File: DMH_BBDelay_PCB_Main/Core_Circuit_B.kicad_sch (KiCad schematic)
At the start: 76 parts, among them J30 Conn_01x08, J31 Conn_01x08, J32 Conn_01x08, J33 Conn_01x08, Q8 J113, SW1 SW_DPDT_3way_x2, SW2 SW_DPDT_x2, SW4 SW_SPDT, U18 CD4053B, U5 TL074, U6 TL074, U7 V3205, U8 CD4046, U9 40106

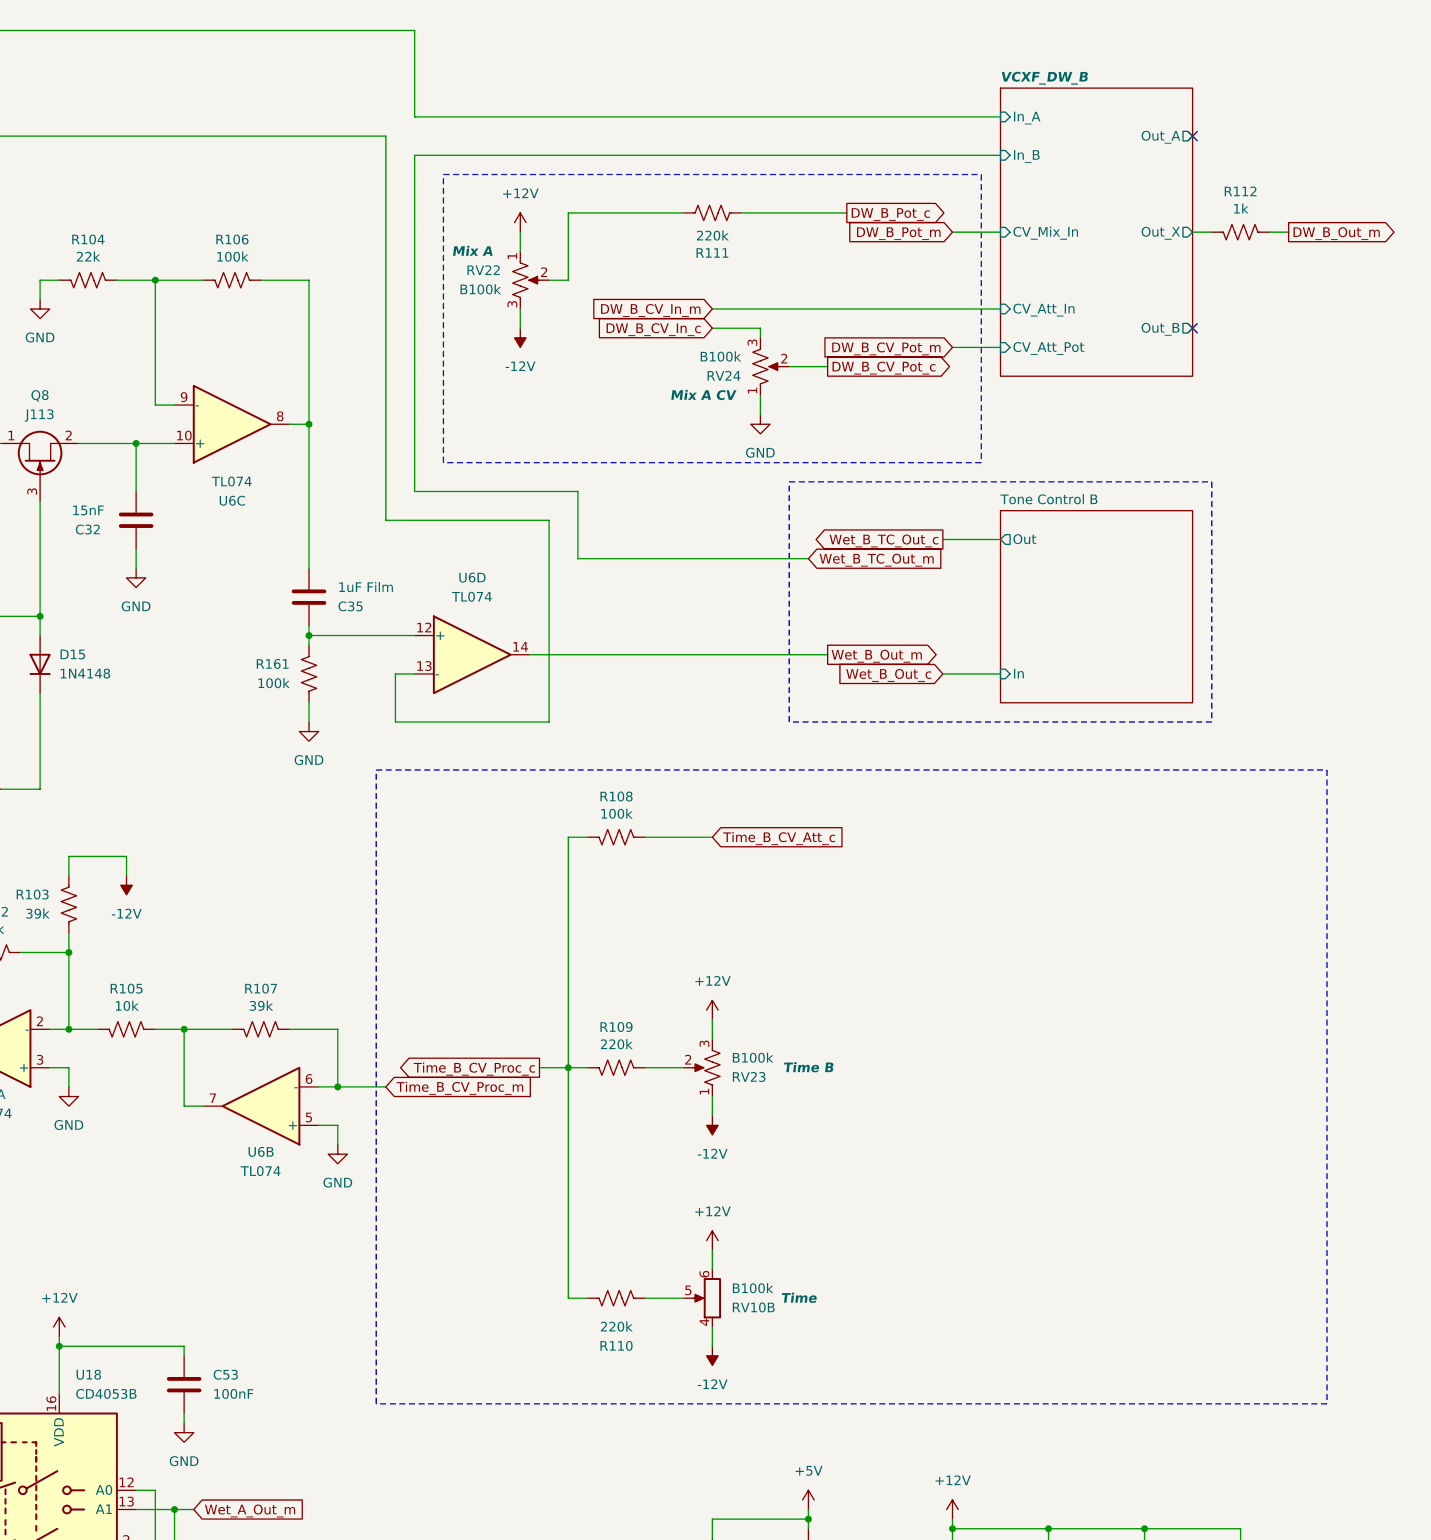
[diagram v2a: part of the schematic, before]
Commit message: Added output filter to channel B
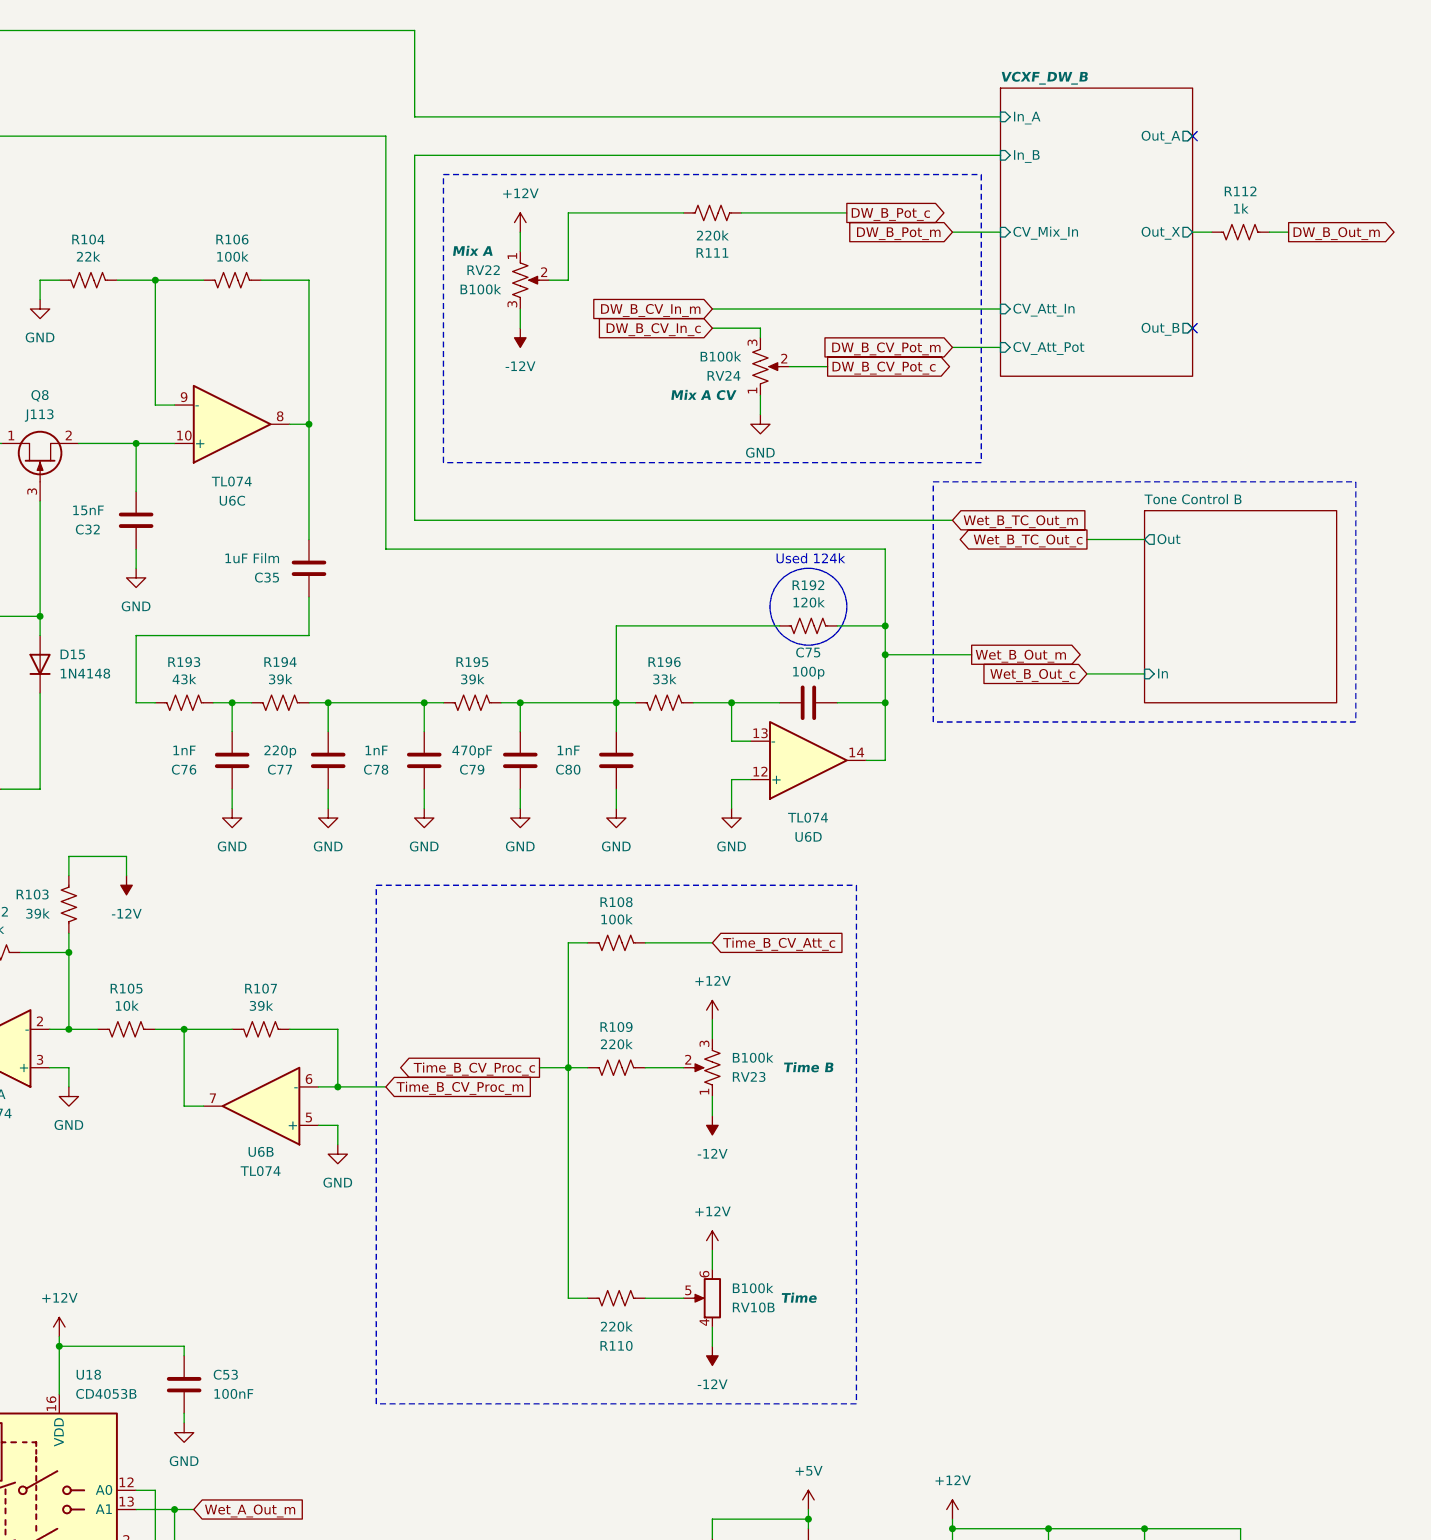
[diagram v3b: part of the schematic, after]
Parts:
- removed R161: 100k, Resistor_THT:R_Axial_DIN0207_L6.3mm_D2.5mm_P7.62mm_Horizontal, symbol Device:R_US
- added C75: 100p, Capacitor_THT:C_Disc_D3.0mm_W2.0mm_P2.50mm, symbol Device:C
- added C76, C78, C80: 1nF, Capacitor_THT:C_Disc_D4.3mm_W1.9mm_P5.00mm, symbol Device:C
- added C77: 220p, Capacitor_THT:C_Disc_D4.3mm_W1.9mm_P5.00mm, symbol Device:C
- added C79: 470pF, Capacitor_THT:C_Disc_D4.3mm_W1.9mm_P5.00mm, symbol Device:C
- added R192: 120k, Resistor_THT:R_Axial_DIN0207_L6.3mm_D2.5mm_P7.62mm_Horizontal, symbol Device:R_US
- added R193: 43k, Resistor_THT:R_Axial_DIN0207_L6.3mm_D2.5mm_P7.62mm_Horizontal, symbol Device:R_US
- added R194, R195: 39k, Resistor_THT:R_Axial_DIN0207_L6.3mm_D2.5mm_P7.62mm_Horizontal, symbol Device:R_US
- added R196: 33k, Resistor_THT:R_Axial_DIN0207_L6.3mm_D2.5mm_P7.62mm_Horizontal, symbol Device:R_US
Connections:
- net GND: now also U6.12 (+), C76.1, C77.1, C78.1, C79.1, C80.1
- net Wet_B_Out_m: now also C75.2, R192.2; no longer U6.13 (-)
- net at C35.1: now also R193.1; no longer U6.12 (+)
- new net: C79.2, C80.2, R192.1, R195.2, R196.1
- new net: C75.1, R196.2, U6.13 (-)
- new net: C77.2, C78.2, R194.2, R195.1
- new net: C76.2, R193.2, R194.1
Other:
- note added: "Used 124k"
- moved on the sheet: C35, R108, U6D

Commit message: Updated internal gains
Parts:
- R104: value 22k -> 18k
- R106: value 100k -> 120k
- R26: value 82k -> 100k
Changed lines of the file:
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@@
 		)
 	)
+	(circle
+		(center 253.746 49.276)
+		(radius 5.08)
+		(stroke
+			(width 0)
+			(type default)
+		)
+		(fill
+			(type none)
+		)
+	)
 	(rectangle
 		(start 45.72 106.68)
@@
 	(text "Used 124k"
 		(exclude_from_sim no)
+		(at 254 43.18 0)
+		(effects
+			(font
+				(size 1.27 1.27)
+			)
+		)
+	)
+	(text "Used 124k"
+		(exclude_from_sim no)
 		(at 330.454 87.884 0)
 		(effects
@@
 			)
 		)
-		(property "Value" "82k"
+		(property "Value" "100k"
 			(at 73.66 77.4699 0)
 			(show_name no)
@@
 			)
 		)
-		(property "Value" "22k"
+		(property "Value" "18k"
 			(at 234.95 47.752 90)
 			(show_name no)
@@
 			)
 		)
-		(property "Value" "100k"
+		(property "Value" "120k"
 			(at 254 47.752 90)
 			(show_name no)

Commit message: Inverted time and tone control pots
... and added AC coupling to the outputs
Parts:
- added C82: 1uF Film, Capacitor_THT:C_Disc_D7.5mm_W5.0mm_P5.00mm, symbol Device:C
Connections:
- net +12V: now also RV10.4, RV23.1; no longer RV10.6, RV23.3
- net -12V: now also RV10.6, RV23.3; no longer RV10.4, RV23.1
- net VCXF_DW_B/Out_X: now also C82.1; no longer R112.1
- new net: C82.2, R112.1
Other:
- moved on the sheet: R112, RV10B, RV23
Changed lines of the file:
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@@
 	(wire
 		(pts
+			(xy 391.16 44.45) (xy 396.24 44.45)
+		)
+		(stroke
+			(width 0)
+			(type default)
+		)
+	)
+	(wire
+		(pts
 			(xy 184.15 162.56) (xy 184.15 165.1)
 		)
@@
 	(wire
 		(pts
-			(xy 381 44.45) (xy 383.54 44.45)
-		)
-		(stroke
-			(width 0)
-			(type default)
-		)
-	)
-	(wire
-		(pts
 			(xy 165.1 31.75) (xy 171.45 31.75)
 		)
@@
 	(wire
 		(pts
-			(xy 391.16 44.45) (xy 393.7 44.45)
-		)
-		(stroke
-			(width 0)
-			(type default)
-		)
-	)
-	(wire
-		(pts
 			(xy 198.12 198.12) (xy 198.12 203.2)
 		)
@@
 	(wire
 		(pts
+			(xy 406.4 50.8) (xy 406.4 44.45)
+		)
+		(stroke
+			(width 0)
+			(type default)
+		)
+	)
+	(wire
+		(pts
 			(xy 177.8 80.01) (xy 177.8 82.55)
 		)
@@
 	(wire
 		(pts
+			(xy 393.7 57.15) (xy 391.16 57.15)
+		)
+		(stroke
+			(width 0)
+			(type default)
+		)
+	)
+	(wire
+		(pts
 			(xy 110.49 111.76) (xy 113.03 111.76)
 		)
@@
 	(wire
 		(pts
+			(xy 381 44.45) (xy 383.54 44.45)
+		)
+		(stroke
+			(width 0)
+			(type default)
+		)
+	)
+	(wire
+		(pts
 			(xy 139.7 31.75) (xy 76.2 31.75)
 		)
@@
 	(wire
 		(pts
+			(xy 391.16 50.8) (xy 406.4 50.8)
+		)
+		(stroke
+			(width 0)
+			(type default)
+		)
+	)
+	(wire
+		(pts
 			(xy 184.15 102.87) (xy 186.69 102.87)
 		)
@@
 	(wire
 		(pts
+			(xy 391.16 57.15) (xy 391.16 50.8)
+		)
+		(stroke
+			(width 0)
+			(type default)
+		)
+	)
+	(wire
+		(pts
 			(xy 304.8 118.11) (xy 304.8 120.65)
 		)
@@
 	(wire
 		(pts
+			(xy 403.86 44.45) (xy 406.4 44.45)
+		)
+		(stroke
+			(width 0)
+			(type default)
+		)
+	)
+	(wire
+		(pts
 			(xy 107.95 71.12) (xy 107.95 67.31)
 		)
@@
 	(global_label "DW_B_Out_m"
 		(shape output)
-		(at 393.7 44.45 0)
+		(at 393.7 57.15 0)
 		(fields_autoplaced yes)
 		(effects
@@
 		)
 		(property "Intersheetrefs" "${INTERSHEET_REFS}"
-			(at 408.2965 44.45 0)
+			(at 408.2965 57.15 0)
 			(hide yes)
 			(show_name no)
@@
 	(symbol
 		(lib_id "Device:R_Potentiometer_US")
-		(at 317.5 154.94 180)
+		(at 317.5 154.94 0)
+		(mirror y)
 		(unit 1)
 		(body_style 1)
@@
 		(dnp no)
 		(property "Reference" "RV23"
-			(at 320.04 156.2101 0)
+			(at 320.04 153.6699 0)
 			(show_name no)
 			(do_not_autoplace no)
@@
 		)
 		(property "Value" "B100k"
-			(at 320.04 153.6701 0)
+			(at 320.04 156.2099 0)
 			(show_name no)
 			(do_not_autoplace no)
@@
 	)
 	(symbol
+		(lib_id "Device:C")
+		(at 387.35 44.45 90)
+		(unit 1)
+		(body_style 1)
+		(exclude_from_sim no)
+		(in_bom yes)
+		(on_board yes)
+		(in_pos_files yes)
+		(dnp no)
+		(property "Reference" "C82"
+			(at 387.35 37.846 90)
+			(show_name no)
+			(do_not_autoplace no)
+			(effects
+				(font
+					(size 1.27 1.27)
+				)
+			)
+		)
+		(property "Value" "1uF Film"
+			(at 387.35 40.386 90)
+			(show_name no)
+			(do_not_autoplace no)
+			(effects
+				(font
+					(size 1.27 1.27)
+				)
+			)
+		)
+		(property "Footprint" "Capacitor_THT:C_Disc_D7.5mm_W5.0mm_P5.00mm"
+			(at 391.16 43.4848 0)
+			(hide yes)
+			(show_name no)
+			(do_not_autoplace no)
+			(effects
+				(font
+					(size 1.27 1.27)
+				)
+			)
+		)
+		(property "Datasheet" ""
+			(at 387.35 44.45 0)
+			(hide yes)
+			(show_name no)
+			(do_not_autoplace no)
+			(effects
+				(font
+					(size 1.27 1.27)
+				)
+			)
+		)
+		(property "Description" "Unpolarized capacitor"
+			(at 387.35 44.45 0)
+			(hide yes)
+			(show_name no)
+			(do_not_autoplace no)
+			(effects
+				(font
+					(size 1.27 1.27)
+				)
+			)
+		)
+		(property "Function" ""
+			(at 387.35 44.45 0)
+			(show_name no)
+			(do_not_autoplace no)
+			(effects
+				(font
+					(size 1.27 1.27)
+				)
+			)
+		)
+		(pin "1"
+		)
+		(pin "2"
+		)
+		(instances
+			(project "DMH_BBDelay_PCB_Main"
+				(path "/58f4306d-5387-4983-bb08-41a2313fd315/53120047-129a-4e0f-876f-6cafa2f18733"
+					(reference "C82")
+					(unit 1)
+				)
+			)
+		)
+	)
+	(symbol
 		(lib_id "Switch:SW_SPDT")
 		(at 96.52 144.78 180)
@@
 	(symbol
 		(lib_id "Device:R_US")
-		(at 387.35 44.45 90)
+		(at 400.05 44.45 90)
 		(mirror x)
 		(unit 1)
@@
 		(dnp no)
 		(property "Reference" "R112"
-			(at 387.35 39.116 90)
+			(at 400.05 39.116 90)
 			(show_name no)
 			(do_not_autoplace no)
@@
 		)
 		(property "Value" "1k"
-			(at 387.35 41.402 90)
+			(at 400.05 41.402 90)
 			(show_name no)
 			(do_not_autoplace no)
@@
 		)
 		(property "Footprint" "Resistor_THT:R_Axial_DIN0207_L6.3mm_D2.5mm_P7.62mm_Horizontal"
-			(at 387.604 45.466 90)
+			(at 400.304 45.466 90)
 			(hide yes)
 			(show_name no)
@@
 		)
 		(property "Datasheet" ""
-			(at 387.35 44.45 0)
+			(at 400.05 44.45 0)
 			(hide yes)
 			(show_name no)
@@
 		)
 		(property "Description" "Resistor, US symbol"
-			(at 387.35 44.45 0)
+			(at 400.05 44.45 0)
 			(hide yes)
 			(show_name no)
@@
 	(symbol
 		(lib_id "Device:R_Potentiometer_Dual_Separate")
-		(at 317.5 185.42 180)
+		(at 317.5 185.42 0)
+		(mirror y)
 		(unit 2)
 		(body_style 1)
@@
 		(dnp no)
 		(property "Reference" "RV10"
-			(at 320.04 186.6901 0)
+			(at 320.04 184.1499 0)
 			(show_name no)
 			(do_not_autoplace no)
@@
 		)
 		(property "Value" "B100k"
-			(at 320.04 184.1501 0)
+			(at 320.04 186.6899 0)
 			(show_name no)
 			(do_not_autoplace no)

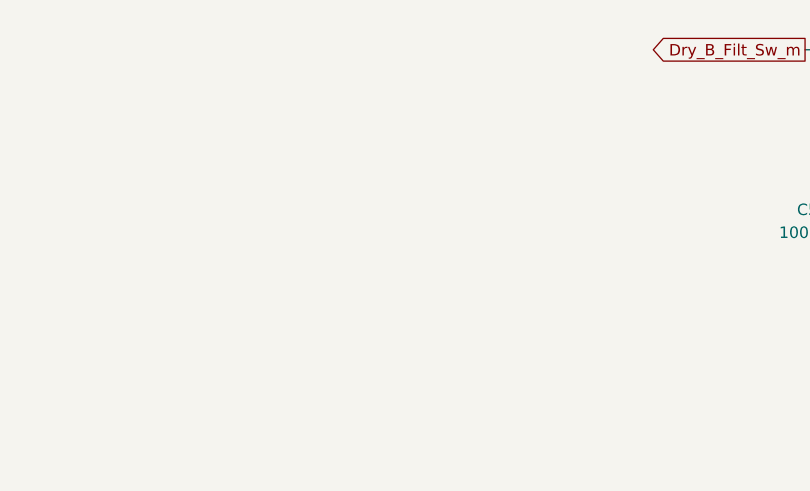
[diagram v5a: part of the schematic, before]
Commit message: Designed input compressor circuits
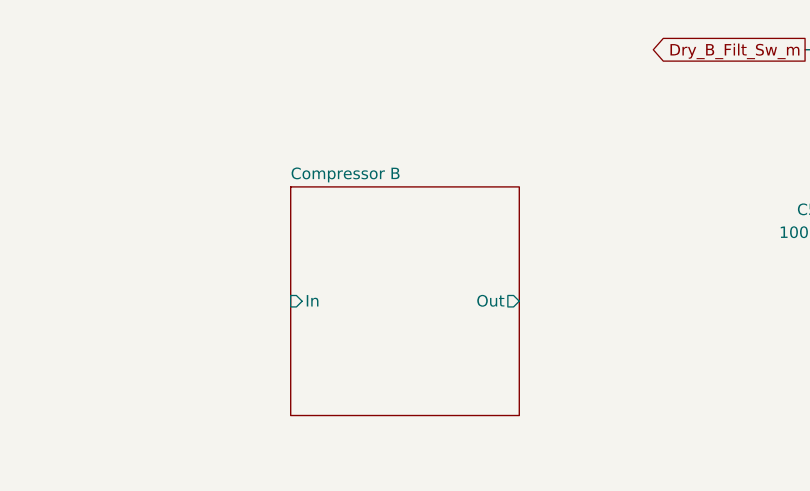
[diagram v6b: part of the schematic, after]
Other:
- added sheet Compressor B (Compressor_B.kicad_sch)
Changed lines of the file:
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@@
+		)
+	)
+	(sheet
+		(at 152.4 241.3)
+		(size 25.4 25.4)
+		(exclude_from_sim no)
+		(in_bom yes)
+		(on_board yes)
+		(dnp no)
+		(fields_autoplaced yes)
+		(stroke
+			(width 0.1524)
+			(type solid)
+		)
+		(fill
+			(color 0 0 0 0)
+		)
+		(property "Sheetname" "Compressor B"
+			(at 152.4 240.5884 0)
+			(show_name no)
+			(do_not_autoplace no)
+			(effects
+				(font
+					(size 1.27 1.27)
+				)
+				(justify left bottom)
+			)
+		)
+		(property "Sheetfile" "Compressor_B.kicad_sch"
+			(at 152.4 267.2846 0)
+			(hide yes)
+			(show_name no)
+			(do_not_autoplace no)
+			(effects
+				(font
+					(size 1.27 1.27)
+				)
+				(justify left top)
+			)
+		)
+		(pin "In" input
+			(at 152.4 254 180)
+			(effects
+				(font
+					(size 1.27 1.27)
+				)
+				(justify left)
+			)
+		)
+		(pin "Out" output
+			(at 177.8 254 0)
+			(effects
+				(font
+					(size 1.27 1.27)
+				)
+				(justify right)
+			)
+		)
+		(instances
+			(project "DMH_BBDelay_PCB_Main"
+				(path "/58f4306d-5387-4983-bb08-41a2313fd315/53120047-129a-4e0f-876f-6cafa2f18733"
+					(page "16")
+				)
+			)
 		)
 	)
